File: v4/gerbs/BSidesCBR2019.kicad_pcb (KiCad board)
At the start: 2 copper layers, 44.9 x 114.1 mm, 26 parts, among them J1 SAO, J2 LSAO, J3 CONN_01X08, SW1 RESET, SW3 <<, SW4 O, SW5 >>, U1 ATMEGA328P-AU, U2 Nokia_5110_LCD, Y1 16Mhz

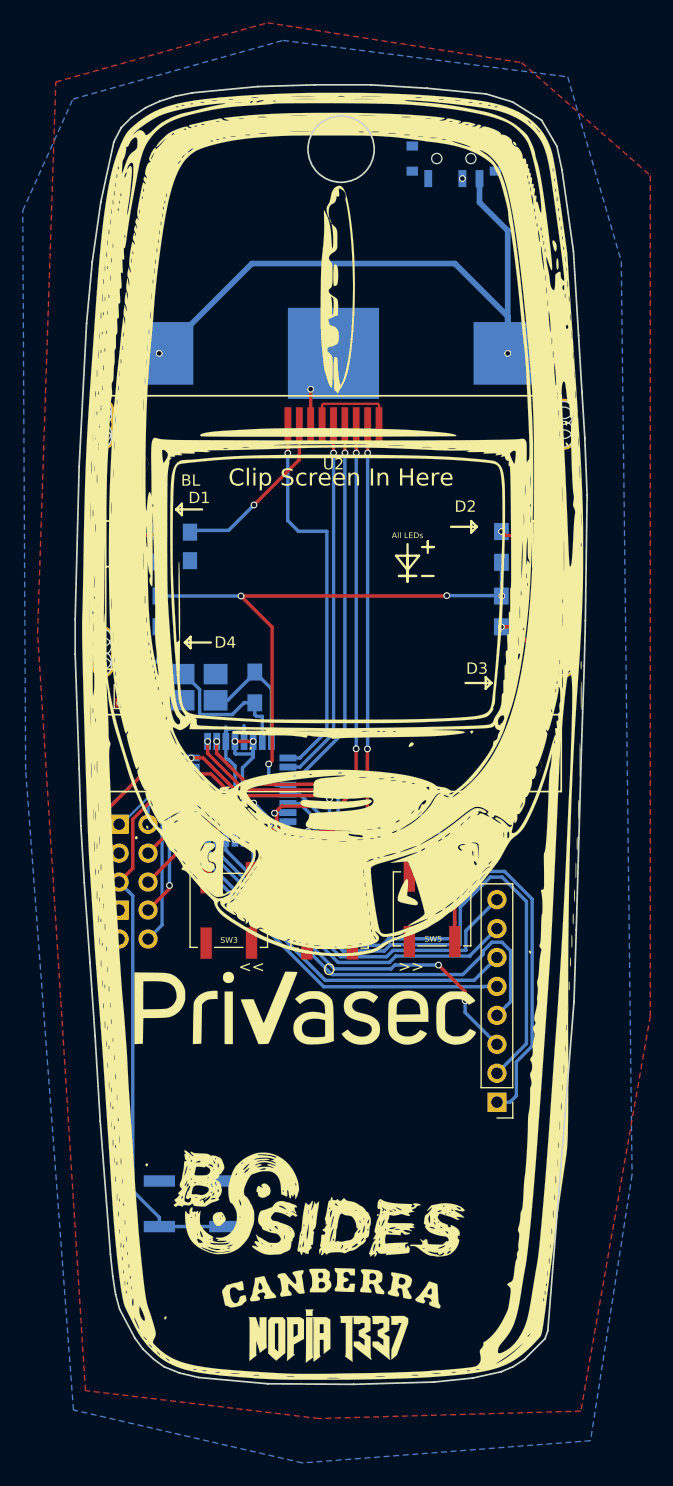
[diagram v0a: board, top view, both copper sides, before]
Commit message: Fixes for buttons, added more silkscreen
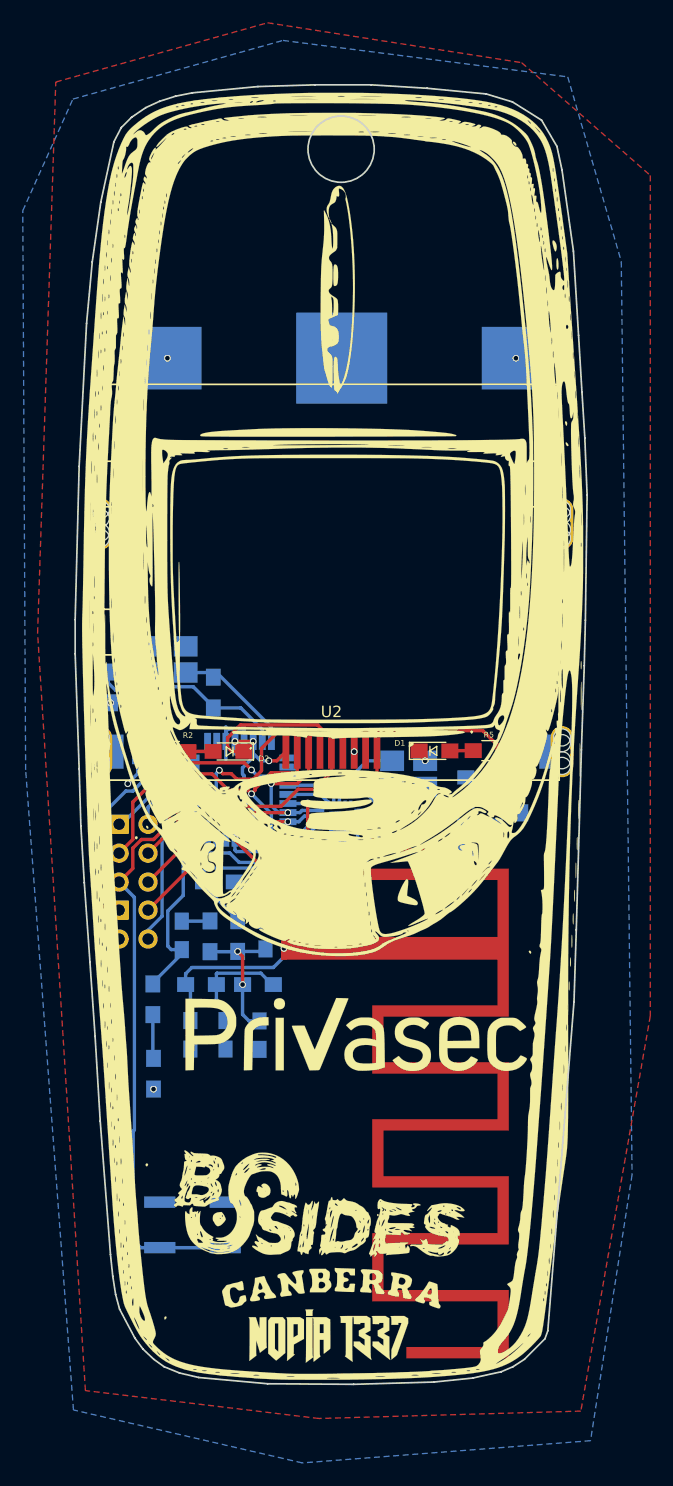
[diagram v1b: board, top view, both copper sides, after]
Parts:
- removed D3, D4: BL, LEDs:LED_0603
- removed the G*** at (42.1, 114.0)
- removed the G*** at (56.8, 125.1)
- removed J3: CONN_01X08, Pin_Headers:Pin_Header_Straight_1x08_Pitch2.54mm
- removed POWER: SW_SPST, Buttons_Switches_SMD:SW_SPDT_PCM12
- removed R6: LR, Resistors_SMD:R_0805_HandSoldering
- removed SW3: <<, Buttons_Switches_SMD:SW_SPST_B3SL-1002P
- removed SW4: O, Buttons_Switches_SMD:SW_SPST_B3SL-1002P
- removed SW5: >>, Buttons_Switches_SMD:SW_SPST_B3SL-1002P
- added AE1: Antenna_Dipole, dipole:ti-dn023-antenna, F.Cu at (54.7, 112.8)
- added C0: , Capacitors_SMD:C_0805_HandSoldering, B.Cu at (46.0, 118.7)
- added C2: , Capacitors_SMD:C_0805_HandSoldering, B.Cu at (72.2, 106.9)
- added C3: , Capacitors_SMD:C_0805_HandSoldering, B.Cu at (72.2, 104.8)
- added C4: , Capacitors_SMD:C_0805_HandSoldering, B.Cu at (72.1, 109.0)
- added CM1: , Capacitors_SMD:C_0805_HandSoldering, B.Cu at (52.8, 127.4)
- added CM2: , Capacitors_SMD:C_0805_HandSoldering, B.Cu at (49.8, 127.4)
- added CM3: , Capacitors_SMD:C_0805_HandSoldering, B.Cu at (46.7, 127.4)
- added CR1: , Capacitors_SMD:C_0805_HandSoldering, B.Cu at (69.6, 111.2)
- added CR2: , Capacitors_SMD:C_0805_HandSoldering, B.Cu at (53.3, 118.6)
- added D5: 1N4148, Diodes_SMD:D_SOD-323_HandSoldering, B.Cu at (43.3, 103.2)
- added G***: LOGO, LOGO, B.Cu at (41.9, 114.0)
- added G***: LOGO, LOGO, F.Cu at (61.3, 127.4)
- added IC1: Si4455-B1A-FM, Si4455-B1A-FM:QFN50P300X300X80-21N-D, B.Cu at (59.8, 108.7)
- added L0: , Inductors_SMD:L_0805_HandSoldering, B.Cu at (48.4, 118.8)
- added LM1: , Inductors_SMD:L_0805_HandSoldering, B.Cu at (52.6, 123.0)
- added LM2: , Inductors_SMD:L_0805_HandSoldering, B.Cu at (47.6, 123.0)
- added LR1: , Inductors_SMD:L_0805_HandSoldering, B.Cu at (49.2, 114.0)
- added LR2: , Inductors_SMD:L_0805_HandSoldering, B.Cu at (50.9, 118.7)
- added Lchoke1: , Inductors_SMD:L_0805_HandSoldering, B.Cu at (43.4, 124.3)
- added ROC1: , Resistors_SMD:R_0805_HandSoldering, B.Cu at (43.5, 130.8)
- added Y2: 30Mhz, Crystals:Crystal_SMD_TXC_7M-4pin_3.2x2.5mm_HandSoldering, B.Cu at (65.9, 104.5)
- BT1: value Battery_Cell -> CR2450
- C1: value 100n -> (none)
- D1, D2: footprint LEDs:LED_0603 -> LEDs:LED_0805_HandSoldering
- R2, R5: moved to F.Cu
- R3: value LR -> 1K
- R4: value 10K -> 1M
- moved C1 36.5 mm to (75.8, 106.7)
- moved U2 33.8 mm to (59.1, 105.0), turned to 180 degrees
- moved D2 33.3 mm to (50.1, 102.5), turned to 180 degrees
- moved D1 33.1 mm to (68.2, 102.5), turned to 0 degrees
- moved R3 32.0 mm to (43.4, 99.5), turned to 90 degrees
- moved R2 18.0 mm to (45.1, 102.5), turned to 180 degrees
- moved R5 17.9 mm to (72.9, 102.5), turned to 180 degrees
- moved R4 5.74 mm to (39.7, 96.9), turned to 270 degrees
- moved R1 3.67 mm to (48.7, 97.4)
- moved Y1 3.59 mm to (44.9, 94.5)
- moved SW1 1.85 mm to (46.9, 144.1)
- moved BT1 0.83 mm to (60.0, 68.0)
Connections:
- BT1 pad 1: BAT+ -> +3.3v
- C1 pad 1: /VOUT -> +3.3v
- D2 pad 1: GND -> Net-(D2-Pad1)
- R2 pad 1: LCDBL+ -> Net-(D2-Pad2)
- R2 pad 2: Net-(D1-Pad2) -> LCDBL+
- R3 pad 1: LCDBL+ -> RESET
- R3 pad 2: Net-(D3-Pad2) -> GND
- R5 pad 1: LCDBL+ -> Net-(D2-Pad1)
- R5 pad 2: Net-(D2-Pad2) -> Net-(D1-Pad2)
- U1 pad 1: BUTTONOK -> Net-(U1-Pad1)
- U1 pad 10: LCDCE -> Net-(U1-Pad10)
- U1 pad 11: LCDDC -> LCDBL+
- U1 pad 12: LCDBL+ -> LCDRST
- U1 pad 13: D9 -> RFNSEL
- U1 pad 14: D10 -> RFNIRQ
- U1 pad 19: A6 -> Net-(U1-Pad19)
- U1 pad 2: BUTTONR -> Net-(U1-Pad2)
- U1 pad 22: A7 -> Net-(U1-Pad22)
- U1 pad 23: AD0 -> Net-(U1-Pad23)
- U1 pad 24: AD1 -> LCDCE
- U1 pad 25: AD2 -> Net-(U1-Pad25)
- U1 pad 26: AD3 -> LCDDC
- U1 pad 32: BUTTONL -> Net-(U1-Pad32)
- U1 pad 9: LCDRST -> Net-(U1-Pad9)
- U2 pad 2: /VOUT -> Net-(U2-Pad2)
- U2 pad 4: +3.3v -> Net-(U2-Pad4)
- Y1 pad 4: GND -> (no net)
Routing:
- net D9: track 60.1 -> 0.00 mm
- net D10: track 55.9 -> 0.00 mm
- net BAT+: track 55.4 -> 0.00 mm, vias 2 -> 0
- net LCDBL+: track 55.2 -> 12.4 mm, vias 4 -> 1
- net AD1: track 40.0 -> 0.00 mm
- net AD3: track 36.9 -> 0.00 mm
- net AD2: track 35.0 -> 0.00 mm
- net AD0: track 34.1 -> 0.00 mm, vias 2 -> 0
- net SCK: track 66.6 -> 33.6 mm, vias 5 -> 2
- net BUTTONR: track 32.8 -> 0.00 mm, vias 3 -> 0
- net BUTTONL: track 31.9 -> 0.00 mm, vias 3 -> 0
- net /TXA: track 0.00 -> 31.7 mm
- net A6: track 30.4 -> 0.00 mm
- net A7: track 30.2 -> 0.00 mm
- net /RXN: track 0.00 -> 30.0 mm, vias 0 -> 2
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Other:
- net class SupaThicc removed
- net class Thinz removed
- board text added: "ĕ'kō (ec0) csirac2 Peter"
- board text removed: "A6"
- board text removed: "A7"
- board text removed: "AD0"
- board text removed: "AD1"
- board text removed: "AD2"
- board text removed: "AD3"
- board text removed: "All LEDs"
- board text removed: "Clip Screen In Here"
- board text removed: "D10"
- board text removed: "D9"
- board text removed: "ec0 (ĕ'kō) csirac2 Peter"
